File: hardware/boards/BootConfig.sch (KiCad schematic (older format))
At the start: 1 part

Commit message: Updated part mfr and added the proper part numbers
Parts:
- U?: MFR (none) -> Lattice; MPN (none) -> LFE5UM5G-85F-8BG381I
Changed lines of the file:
@@
 $Descr A4 11693 8268
 encoding utf-8
-Sheet 8 11
+Sheet 7 11
 Title ""
 Date ""
@@
 F 2 "" H 4550 1650 50  0001 C CNN
 F 3 "" H 4550 1650 50  0001 C CNN
+F 4 "Lattice" H 5900 1500 50  0001 C CNN "MFR"
+F 5 "LFE5UM5G-85F-8BG381I" H 5900 1500 50  0001 C CNN "MPN"
 	8    5900 1500
 	1    0    0    -1

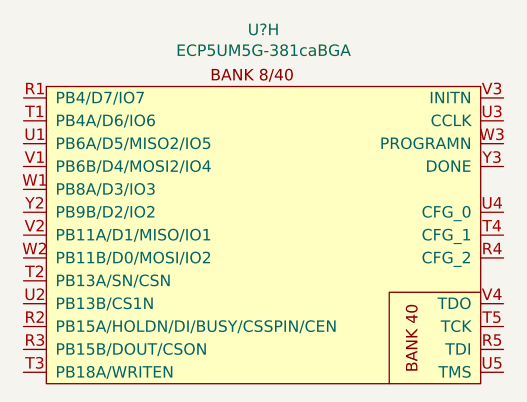
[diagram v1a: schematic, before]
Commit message: Did some annotation and fixed the FPGA bank that was accidentally labled as the cypress part
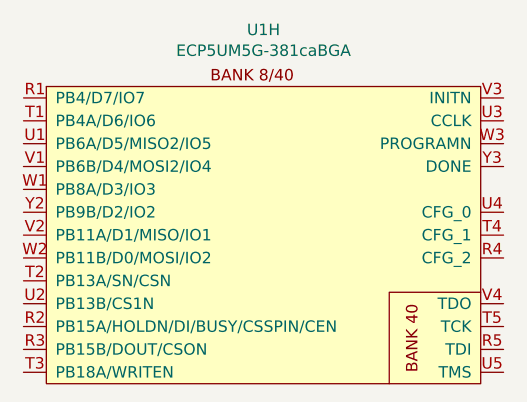
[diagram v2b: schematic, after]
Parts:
- U1: renamed from U?; footprint (none) -> lethalbit:318caBGA
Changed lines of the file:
@@
 AR Path="/5F21A733" Ref="U?"  Part="8"
 AR Path="/5EF66188/5F21A733" Ref="U?"  Part="8"
-AR Path="/5EF66251/5F21A733" Ref="U?"  Part="8"
-F 0 "U?" H 5950 1848 50  0000 C CNN
+AR Path="/5EF66251/5F21A733" Ref="U1"  Part="8"
+F 0 "U1" H 5950 1848 50  0000 C CNN
 F 1 "ECP5UM5G-381caBGA" H 5950 1757 50  0000 C CNN
-F 2 "" H 4550 1650 50  0001 C CNN
+F 2 "lethalbit:318caBGA" H 4550 1650 50  0001 C CNN
 F 3 "" H 4550 1650 50  0001 C CNN
 F 4 "Lattice" H 5900 1500 50  0001 C CNN "MFR"

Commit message: Some more mist schematic edits
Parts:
- U1: DIGIKEY_PN (none) -> 220-2112-ND
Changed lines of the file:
@@
 F 4 "Lattice" H 5900 1500 50  0001 C CNN "MFR"
 F 5 "LFE5UM5G-85F-8BG381I" H 5900 1500 50  0001 C CNN "MPN"
+F 6 "220-2112-ND" H 5900 1500 50  0001 C CNN "DIGIKEY_PN"
 	8    5900 1500
 	1    0    0    -1

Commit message: Some strugglebusting on getting the ERC errors cleaned up a bit
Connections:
- no-connect marks 0 -> 24
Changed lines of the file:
@@
 $Descr A4 11693 8268
 encoding utf-8
-Sheet 7 10
+Sheet 9 10
 Title "lethallink"
 Date "2020-06-13"
@@
 	1    0    0    -1
 $EndComp
+NoConn ~ 4900 1450
+NoConn ~ 4900 1550
+NoConn ~ 4900 1650
+NoConn ~ 4900 1750
+NoConn ~ 4900 1850
+NoConn ~ 4900 1950
+NoConn ~ 4900 2050
+NoConn ~ 4900 2150
+NoConn ~ 4900 2250
+NoConn ~ 4900 2350
+NoConn ~ 4900 2450
+NoConn ~ 4900 2550
+NoConn ~ 4900 2650
+NoConn ~ 7000 2650
+NoConn ~ 7000 2550
+NoConn ~ 7000 2450
+NoConn ~ 7000 2350
+NoConn ~ 7000 2150
+NoConn ~ 7000 2050
+NoConn ~ 7000 1950
+NoConn ~ 7000 1750
+NoConn ~ 7000 1650
+NoConn ~ 7000 1550
+NoConn ~ 7000 1450
 $EndSCHEMATC
